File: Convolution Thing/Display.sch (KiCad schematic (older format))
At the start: 5 parts

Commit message: Added gate inputs and CM4 / display sockets, made CV inputs 100k, lots of smaller changes. First iteration of schematic now done.
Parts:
- added C?: 100nF, symbol Device:C
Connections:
- net +12V: now also C?.1
- net GND: now also C?.2
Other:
- moved on the sheet: C?, R?

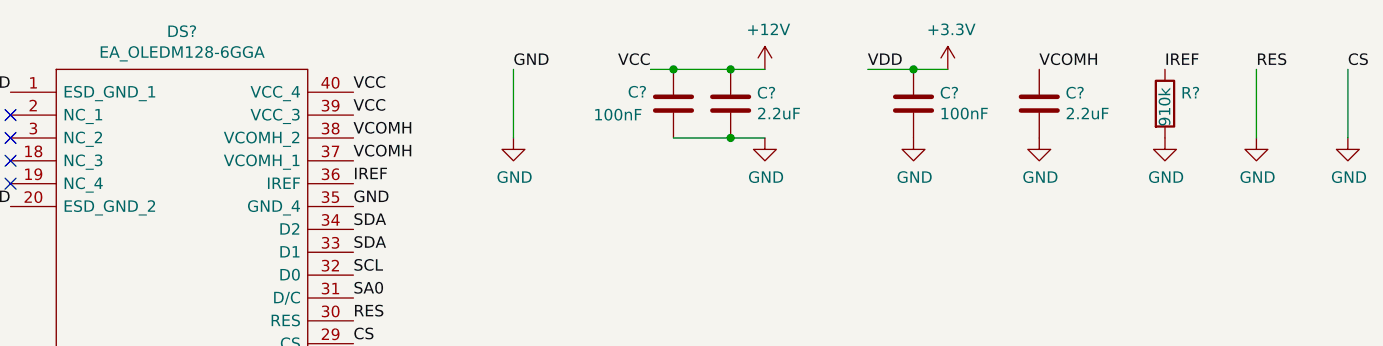
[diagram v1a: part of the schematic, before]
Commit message: Fix some issues, add component references
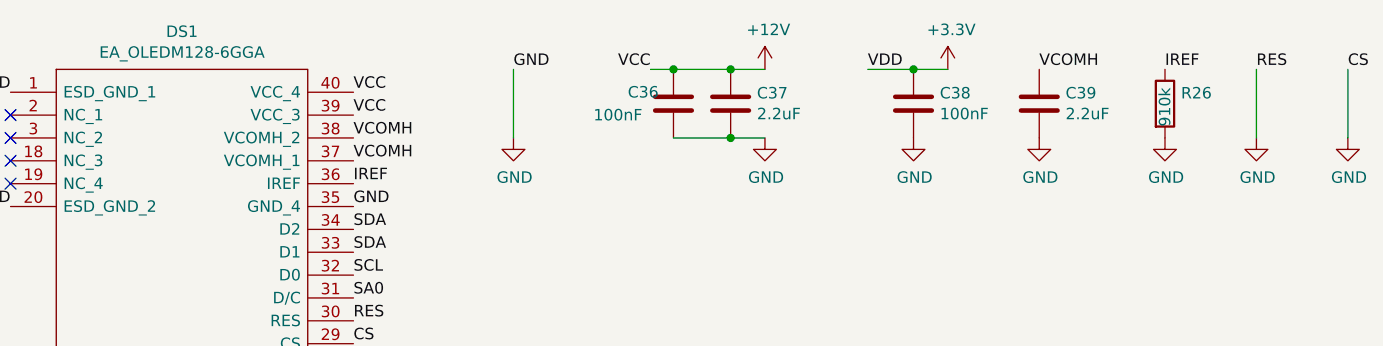
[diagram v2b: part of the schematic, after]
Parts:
- gave numbers to parts that had none: 6
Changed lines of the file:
@@
 $EndDescr
 $Comp
-L SamacSys:EA_OLEDM128-6GGA DS?
+L SamacSys:EA_OLEDM128-6GGA DS1
 U 1 1 61136657
 P 1300 1100
-F 0 "DS?" H 2050 1365 50  0000 C CNN
+F 0 "DS1" H 2050 1365 50  0000 C CNN
 F 1 "EA_OLEDM128-6GGA" H 2050 1274 50  0000 C CNN
 F 2 "EAOLEDM1286GGA" H 2650 1200 50  0001 L CNN
@@
 GND
 $Comp
-L power:GND #PWR?
+L power:GND #PWR065
 U 1 1 6113B02C
 P 3500 1300
-F 0 "#PWR?" H 3500 1050 50  0001 C CNN
+F 0 "#PWR065" H 3500 1050 50  0001 C CNN
 F 1 "GND" H 3505 1127 50  0000 C CNN
 F 2 "" H 3500 1300 50  0001 C CNN
@@
 VCC
 $Comp
-L Device:C C?
+L Device:C C37
 U 1 1 6113CBE1
 P 4450 1150
-F 0 "C?" H 4565 1196 50  0000 L CNN
+F 0 "C37" H 4565 1196 50  0000 L CNN
 F 1 "2.2uF" H 4565 1105 50  0000 L CNN
 F 2 "" H 4488 1000 50  0001 C CNN
@@
 VDD
 $Comp
-L power:+12V #PWR?
+L power:+12V #PWR066
 U 1 1 611429CC
 P 4600 1000
-F 0 "#PWR?" H 4600 850 50  0001 C CNN
+F 0 "#PWR066" H 4600 850 50  0001 C CNN
 F 1 "+12V" H 4615 1173 50  0000 C CNN
 F 2 "" H 4600 1000 50  0001 C CNN
@@
 VDD
 $Comp
-L Device:C C?
+L Device:C C38
 U 1 1 61144392
 P 5250 1150
-F 0 "C?" H 5365 1196 50  0000 L CNN
+F 0 "C38" H 5365 1196 50  0000 L CNN
 F 1 "100nF" H 5365 1105 50  0000 L CNN
 F 2 "" H 5288 1000 50  0001 C CNN
@@
 $EndComp
 $Comp
-L power:GND #PWR?
+L power:GND #PWR068
 U 1 1 61144398
 P 5250 1300
-F 0 "#PWR?" H 5250 1050 50  0001 C CNN
+F 0 "#PWR068" H 5250 1050 50  0001 C CNN
 F 1 "GND" H 5255 1127 50  0000 C CNN
 F 2 "" H 5250 1300 50  0001 C CNN
@@
 	5250 1000 5050 1000
 $Comp
-L power:+3.3V #PWR?
+L power:+3.3V #PWR069
 U 1 1 611445B1
 P 5400 1000
-F 0 "#PWR?" H 5400 850 50  0001 C CNN
+F 0 "#PWR069" H 5400 850 50  0001 C CNN
 F 1 "+3.3V" H 5415 1173 50  0000 C CNN
 F 2 "" H 5400 1000 50  0001 C CNN
@@
 VCOMH
 $Comp
-L Device:C C?
+L Device:C C39
 U 1 1 61146336
 P 5800 1150
-F 0 "C?" H 5915 1196 50  0000 L CNN
+F 0 "C39" H 5915 1196 50  0000 L CNN
 F 1 "2.2uF" H 5915 1105 50  0000 L CNN
 F 2 "" H 5838 1000 50  0001 C CNN
@@
 $EndComp
 $Comp
-L power:GND #PWR?
+L power:GND #PWR070
 U 1 1 61147221
 P 5800 1300
-F 0 "#PWR?" H 5800 1050 50  0001 C CNN
+F 0 "#PWR070" H 5800 1050 50  0001 C CNN
 F 1 "GND" H 5805 1127 50  0000 C CNN
 F 2 "" H 5800 1300 50  0001 C CNN
@@
 BS0
 $Comp
-L power:+3.3V #PWR?
+L power:+3.3V #PWR074
 U 1 1 61148FFD
 P 8250 1250
-F 0 "#PWR?" H 8250 1100 50  0001 C CNN
+F 0 "#PWR074" H 8250 1100 50  0001 C CNN
 F 1 "+3.3V" H 8265 1423 50  0000 C CNN
 F 2 "" H 8250 1250 50  0001 C CNN
@@
 BS1
 $Comp
-L power:GND #PWR?
+L power:GND #PWR075
 U 1 1 61149488
 P 8250 1400
-F 0 "#PWR?" H 8250 1150 50  0001 C CNN
+F 0 "#PWR075" H 8250 1150 50  0001 C CNN
 F 1 "GND" H 8255 1227 50  0000 C CNN
 F 2 "" H 8250 1400 50  0001 C CNN
@@
 SA0
 $Comp
-L power:GND #PWR?
+L power:GND #PWR076
 U 1 1 6114D0D7
 P 9100 1250
-F 0 "#PWR?" H 9100 1000 50  0001 C CNN
+F 0 "#PWR076" H 9100 1000 50  0001 C CNN
 F 1 "GND" H 9105 1077 50  0000 C CNN
 F 2 "" H 9100 1250 50  0001 C CNN
@@
 IREF
 $Comp
-L Device:R R?
+L Device:R R26
 U 1 1 611577FF
 P 6350 1150
-F 0 "R?" H 6420 1196 50  0000 L CNN
+F 0 "R26" H 6420 1196 50  0000 L CNN
 F 1 "910k" V 6350 1050 50  0000 L CNN
 F 2 "" V 6280 1150 50  0001 C CNN
@@
 $EndComp
 $Comp
-L power:GND #PWR?
+L power:GND #PWR071
 U 1 1 61157B74
 P 6350 1300
-F 0 "#PWR?" H 6350 1050 50  0001 C CNN
+F 0 "#PWR071" H 6350 1050 50  0001 C CNN
 F 1 "GND" H 6355 1127 50  0000 C CNN
 F 2 "" H 6350 1300 50  0001 C CNN
@@
 RES
 $Comp
-L power:GND #PWR?
+L power:GND #PWR072
 U 1 1 6115A75A
 P 6750 1300
-F 0 "#PWR?" H 6750 1050 50  0001 C CNN
+F 0 "#PWR072" H 6750 1050 50  0001 C CNN
 F 1 "GND" H 6755 1127 50  0000 C CNN
 F 2 "" H 6750 1300 50  0001 C CNN
@@
 CS
 $Comp
-L power:GND #PWR?
+L power:GND #PWR073
 U 1 1 6115C743
 P 7150 1300
-F 0 "#PWR?" H 7150 1050 50  0001 C CNN
+F 0 "#PWR073" H 7150 1050 50  0001 C CNN
 F 1 "GND" H 7155 1127 50  0000 C CNN
 F 2 "" H 7150 1300 50  0001 C CNN
@@
 	7150 1300 7150 1000
 $Comp
-L Device:C C?
+L Device:C C36
 U 1 1 612C59AB
 P 4200 1150
-F 0 "C?" H 4000 1200 50  0000 L CNN
+F 0 "C36" H 4000 1200 50  0000 L CNN
 F 1 "100nF" H 3850 1100 50  0000 L CNN
 F 2 "" H 4238 1000 50  0001 C CNN
@@
 Connection ~ 4200 1000
 $Comp
-L power:GND #PWR?
+L power:GND #PWR067
 U 1 1 612C8937
 P 4600 1300
-F 0 "#PWR?" H 4600 1050 50  0001 C CNN
+F 0 "#PWR067" H 4600 1050 50  0001 C CNN
 F 1 "GND" H 4605 1127 50  0000 C CNN
 F 2 "" H 4600 1300 50  0001 C CNN

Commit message: Started footprint assignment
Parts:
- DS1: footprint EAOLEDM1286GGA -> SamacSys:EAOLEDM1286GGA
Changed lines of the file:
@@
 F 0 "DS1" H 2050 1365 50  0000 C CNN
 F 1 "EA_OLEDM128-6GGA" H 2050 1274 50  0000 C CNN
-F 2 "EAOLEDM1286GGA" H 2650 1200 50  0001 L CNN
+F 2 "SamacSys:EAOLEDM1286GGA" H 2650 1200 50  0001 L CNN
 F 3 "https://www.google.com/url?sa=t&rct=j&q=&esrc=s&source=web&cd=&ved=2ahUKEwi74d_O2ZbyAhUKyxoKHT4kDm4QFnoECAkQAw&url=https%3A%2F%2Fwww.lcd-module.com%2Ffileadmin%2Feng%2Fpdf%2Fgrafik%2Foledm128-6e.pdf&usg=AOvVaw1oKrIyqRIy1bW-4cLfrIu6" H 2650 1100 50  0001 L CNN
 F 4 "OLED Displays & Accessories Graphic OLED Yellow 128x64 with glass,," H 2650 1000 50  0001 L CNN "Description"

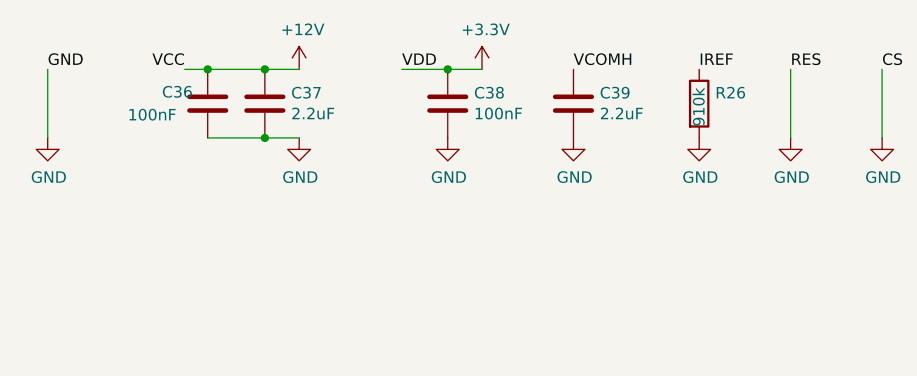
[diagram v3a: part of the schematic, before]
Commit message: Assign all footprints
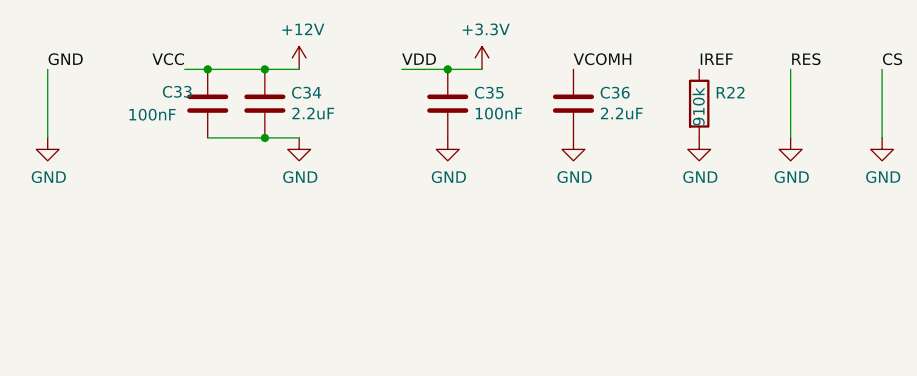
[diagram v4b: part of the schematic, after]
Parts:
- C33: renamed from C36; footprint (none) -> Capacitor_SMD:C_0805_2012Metric
- C34: renamed from C37; footprint (none) -> Capacitor_SMD:C_0805_2012Metric
- C35: renamed from C38; footprint (none) -> Capacitor_SMD:C_0805_2012Metric
- C36: renamed from C39; footprint (none) -> Capacitor_SMD:C_0805_2012Metric
- R22: renamed from R26; footprint (none) -> Resistor_SMD:R_0805_2012Metric
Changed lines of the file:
@@
 GND
 $Comp
-L power:GND #PWR065
+L power:GND #PWR058
 U 1 1 6113B02C
 P 3500 1300
-F 0 "#PWR065" H 3500 1050 50  0001 C CNN
+F 0 "#PWR058" H 3500 1050 50  0001 C CNN
 F 1 "GND" H 3505 1127 50  0000 C CNN
 F 2 "" H 3500 1300 50  0001 C CNN
@@
 VCC
 $Comp
-L Device:C C37
+L Device:C C34
 U 1 1 6113CBE1
 P 4450 1150
-F 0 "C37" H 4565 1196 50  0000 L CNN
+F 0 "C34" H 4565 1196 50  0000 L CNN
 F 1 "2.2uF" H 4565 1105 50  0000 L CNN
-F 2 "" H 4488 1000 50  0001 C CNN
+F 2 "Capacitor_SMD:C_0805_2012Metric" H 4488 1000 50  0001 C CNN
 F 3 "~" H 4450 1150 50  0001 C CNN
 	1    4450 1150
@@
 VDD
 $Comp
-L power:+12V #PWR066
+L power:+12V #PWR059
 U 1 1 611429CC
 P 4600 1000
-F 0 "#PWR066" H 4600 850 50  0001 C CNN
+F 0 "#PWR059" H 4600 850 50  0001 C CNN
 F 1 "+12V" H 4615 1173 50  0000 C CNN
 F 2 "" H 4600 1000 50  0001 C CNN
@@
 VDD
 $Comp
-L Device:C C38
+L Device:C C35
 U 1 1 61144392
 P 5250 1150
-F 0 "C38" H 5365 1196 50  0000 L CNN
+F 0 "C35" H 5365 1196 50  0000 L CNN
 F 1 "100nF" H 5365 1105 50  0000 L CNN
-F 2 "" H 5288 1000 50  0001 C CNN
+F 2 "Capacitor_SMD:C_0805_2012Metric" H 5288 1000 50  0001 C CNN
 F 3 "~" H 5250 1150 50  0001 C CNN
 	1    5250 1150
@@
 $EndComp
 $Comp
-L power:GND #PWR068
+L power:GND #PWR061
 U 1 1 61144398
 P 5250 1300
-F 0 "#PWR068" H 5250 1050 50  0001 C CNN
+F 0 "#PWR061" H 5250 1050 50  0001 C CNN
 F 1 "GND" H 5255 1127 50  0000 C CNN
 F 2 "" H 5250 1300 50  0001 C CNN
@@
 	5250 1000 5050 1000
 $Comp
-L power:+3.3V #PWR069
+L power:+3.3V #PWR062
 U 1 1 611445B1
 P 5400 1000
-F 0 "#PWR069" H 5400 850 50  0001 C CNN
+F 0 "#PWR062" H 5400 850 50  0001 C CNN
 F 1 "+3.3V" H 5415 1173 50  0000 C CNN
 F 2 "" H 5400 1000 50  0001 C CNN
@@
 VCOMH
 $Comp
-L Device:C C39
+L Device:C C36
 U 1 1 61146336
 P 5800 1150
-F 0 "C39" H 5915 1196 50  0000 L CNN
+F 0 "C36" H 5915 1196 50  0000 L CNN
 F 1 "2.2uF" H 5915 1105 50  0000 L CNN
-F 2 "" H 5838 1000 50  0001 C CNN
+F 2 "Capacitor_SMD:C_0805_2012Metric" H 5838 1000 50  0001 C CNN
 F 3 "~" H 5800 1150 50  0001 C CNN
 	1    5800 1150
@@
 $EndComp
 $Comp
-L power:GND #PWR070
+L power:GND #PWR063
 U 1 1 61147221
 P 5800 1300
-F 0 "#PWR070" H 5800 1050 50  0001 C CNN
+F 0 "#PWR063" H 5800 1050 50  0001 C CNN
 F 1 "GND" H 5805 1127 50  0000 C CNN
 F 2 "" H 5800 1300 50  0001 C CNN
@@
 BS0
 $Comp
-L power:+3.3V #PWR074
+L power:+3.3V #PWR067
 U 1 1 61148FFD
 P 8250 1250
-F 0 "#PWR074" H 8250 1100 50  0001 C CNN
+F 0 "#PWR067" H 8250 1100 50  0001 C CNN
 F 1 "+3.3V" H 8265 1423 50  0000 C CNN
 F 2 "" H 8250 1250 50  0001 C CNN
@@
 BS1
 $Comp
-L power:GND #PWR075
+L power:GND #PWR068
 U 1 1 61149488
 P 8250 1400
-F 0 "#PWR075" H 8250 1150 50  0001 C CNN
+F 0 "#PWR068" H 8250 1150 50  0001 C CNN
 F 1 "GND" H 8255 1227 50  0000 C CNN
 F 2 "" H 8250 1400 50  0001 C CNN
@@
 SA0
 $Comp
-L power:GND #PWR076
+L power:GND #PWR069
 U 1 1 6114D0D7
 P 9100 1250
-F 0 "#PWR076" H 9100 1000 50  0001 C CNN
+F 0 "#PWR069" H 9100 1000 50  0001 C CNN
 F 1 "GND" H 9105 1077 50  0000 C CNN
 F 2 "" H 9100 1250 50  0001 C CNN
@@
 IREF
 $Comp
-L Device:R R26
+L Device:R R22
 U 1 1 611577FF
 P 6350 1150
-F 0 "R26" H 6420 1196 50  0000 L CNN
+F 0 "R22" H 6420 1196 50  0000 L CNN
 F 1 "910k" V 6350 1050 50  0000 L CNN
-F 2 "" V 6280 1150 50  0001 C CNN
+F 2 "Resistor_SMD:R_0805_2012Metric" V 6280 1150 50  0001 C CNN
 F 3 "~" H 6350 1150 50  0001 C CNN
 	1    6350 1150
@@
 $EndComp
 $Comp
-L power:GND #PWR071
+L power:GND #PWR064
 U 1 1 61157B74
 P 6350 1300
-F 0 "#PWR071" H 6350 1050 50  0001 C CNN
+F 0 "#PWR064" H 6350 1050 50  0001 C CNN
 F 1 "GND" H 6355 1127 50  0000 C CNN
 F 2 "" H 6350 1300 50  0001 C CNN
@@
 RES
 $Comp
-L power:GND #PWR072
+L power:GND #PWR065
 U 1 1 6115A75A
 P 6750 1300
-F 0 "#PWR072" H 6750 1050 50  0001 C CNN
+F 0 "#PWR065" H 6750 1050 50  0001 C CNN
 F 1 "GND" H 6755 1127 50  0000 C CNN
 F 2 "" H 6750 1300 50  0001 C CNN
@@
 CS
 $Comp
-L power:GND #PWR073
+L power:GND #PWR066
 U 1 1 6115C743
 P 7150 1300
-F 0 "#PWR073" H 7150 1050 50  0001 C CNN
+F 0 "#PWR066" H 7150 1050 50  0001 C CNN
 F 1 "GND" H 7155 1127 50  0000 C CNN
 F 2 "" H 7150 1300 50  0001 C CNN
@@
 	7150 1300 7150 1000
 $Comp
-L Device:C C36
+L Device:C C33
 U 1 1 612C59AB
 P 4200 1150
-F 0 "C36" H 4000 1200 50  0000 L CNN
+F 0 "C33" H 4000 1200 50  0000 L CNN
 F 1 "100nF" H 3850 1100 50  0000 L CNN
-F 2 "" H 4238 1000 50  0001 C CNN
+F 2 "Capacitor_SMD:C_0805_2012Metric" H 4238 1000 50  0001 C CNN
 F 3 "~" H 4200 1150 50  0001 C CNN
 	1    4200 1150
@@
 Connection ~ 4200 1000
 $Comp
-L power:GND #PWR067
+L power:GND #PWR060
 U 1 1 612C8937
 P 4600 1300
-F 0 "#PWR067" H 4600 1050 50  0001 C CNN
+F 0 "#PWR060" H 4600 1050 50  0001 C CNN
 F 1 "GND" H 4605 1127 50  0000 C CNN
 F 2 "" H 4600 1300 50  0001 C CNN

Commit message: PCB layout work and related changes to the schematic
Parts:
- added TP11: DISPLAY_SCL TP, TestPoint:TestPoint_Loop_D2.60mm_Drill1.6mm_Beaded, symbol Connector:TestPoint
- added TP12: DISPLAY_SDA TP, TestPoint:TestPoint_Loop_D2.60mm_Drill1.6mm_Beaded, symbol Connector:TestPoint
- renumbered C33 to C29, C34 to C30, C35 to C31, C36 to C32, R22 to R20
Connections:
- net DISPLAY_SCL renamed CM4_SCL1
- net CM4_SCL1: now also TP11.1
- net DISPLAY_SDA renamed CM4_SDA1
- net CM4_SDA1: now also TP12.1
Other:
- moved on the sheet: C29, C30, C31, C32, DS1, R20
